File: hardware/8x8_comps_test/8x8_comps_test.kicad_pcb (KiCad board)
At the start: 2 copper layers, 408.6 x 315.4 mm, 250 parts

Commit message: Added test Schematic and PCB
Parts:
- removed ADC_3, ADC_4, ADC_5, ADC_6, ADC_7, ADC_8: MCP3008-I/P-DIP16, ADC:MCP3008-I&slash_P
- removed AMP_10, AMP_11, AMP_12, AMP_13, AMP_14, AMP_15, AMP_16, AMP_3, AMP_4, AMP_5, AMP_6, AMP_7, AMP_8, AMP_9: MCP619-I/SL, Op-Amp:footprints
- removed Addr_Sel_2, Addr_Sel_3, Addr_Sel_4, Addr_Sel_5, Addr_Sel_6: 100K, Resistor_THT:R_Axial_DIN0207_L6.3mm_D2.5mm_P7.62mm_Horizontal
- removed Amp_Fdbk_10, Amp_Fdbk_11, Amp_Fdbk_12, Amp_Fdbk_13, Amp_Fdbk_14, Amp_Fdbk_15, Amp_Fdbk_16, Amp_Fdbk_17, Amp_Fdbk_18, Amp_Fdbk_19, Amp_Fdbk_20, Amp_Fdbk_21, Amp_Fdbk_22, Amp_Fdbk_23, Amp_Fdbk_24, Amp_Fdbk_25, Amp_Fdbk_26, Amp_Fdbk_27, Amp_Fdbk_28, Amp_Fdbk_29, Amp_Fdbk_3, Amp_Fdbk_30, Amp_Fdbk_31, Amp_Fdbk_32, Amp_Fdbk_33, Amp_Fdbk_34, Amp_Fdbk_35, Amp_Fdbk_36, Amp_Fdbk_37, Amp_Fdbk_38, Amp_Fdbk_39, Amp_Fdbk_4, Amp_Fdbk_40, Amp_Fdbk_41, Amp_Fdbk_42, Amp_Fdbk_43, Amp_Fdbk_44, Amp_Fdbk_45, Amp_Fdbk_46, Amp_Fdbk_47, Amp_Fdbk_48, Amp_Fdbk_49, Amp_Fdbk_50, Amp_Fdbk_51, Amp_Fdbk_52, Amp_Fdbk_53, Amp_Fdbk_54, Amp_Fdbk_55, Amp_Fdbk_56, Amp_Fdbk_57, Amp_Fdbk_58, Amp_Fdbk_59, Amp_Fdbk_60, Amp_Fdbk_61, Amp_Fdbk_62, Amp_Fdbk_63, Amp_Fdbk_64, Amp_Fdbk_7, Amp_Fdbk_8, Amp_Fdbk_9: 2M, Resistor_THT:R_Axial_DIN0207_L6.3mm_D2.5mm_P7.62mm_Horizontal
- removed Drv_I_Sel_2, Drv_I_Sel_3, Drv_I_Sel_4, Drv_I_Sel_5, Drv_I_Sel_6, Drv_I_Sel_7, Drv_I_Sel_8: 2K, Resistor_THT:R_Axial_DIN0207_L6.3mm_D2.5mm_P7.62mm_Horizontal
- removed Drv_RST_PU_2, Drv_RST_PU_3, Drv_RST_PU_4, Drv_RST_PU_5, Drv_RST_PU_6, Drv_RST_PU_7, Drv_RST_PU_8: 10K, Resistor_THT:R_Axial_DIN0207_L6.3mm_D2.5mm_P7.62mm_Horizontal
- removed LD10, LD11, LD12, LD13, LD14, LD15, LD16, LD17, LD18, LD19, LD20, LD21, LD22, LD23, LD24, LD25, LD26, LD27, LD28, LD29, LD30, LD31, LD32, LD33, LD34, LD35, LD36, LD37, LD38, LD39, LD40, LD41, LD42, LD43, LD44, LD45, LD46, LD47, LD48, LD49, LD5, LD50, LD51, LD52, LD53, LD54, LD55, LD56, LD57, LD58, LD59, LD6, LD60, LD61, LD62, LD63, LD64, LD7, LD8, LD9: WP154A4SEJ3VBDZGC/CA, RGB LED:WP154A4SEJ3VBDZGC&slash_CA
- removed LED_Driver_2, LED_Driver_3, LED_Driver_4, LED_Driver_5, LED_Driver_6, LED_Driver_7, LED_Driver_8: PCA9956BTWY, LED Driver:SOP50P640X110-39N
- removed OC10, OC11, OC12, OC13, OC14, OC15, OC16, OC17, OC18, OC19, OC20, OC21, OC22, OC23, OC24, OC25, OC26, OC27, OC28, OC29, OC30, OC31, OC32, OC33, OC34, OC35, OC36, OC37, OC38, OC39, OC40, OC41, OC42, OC43, OC44, OC45, OC46, OC47, OC48, OC49, OC5, OC50, OC51, OC52, OC53, OC54, OC55, OC56, OC57, OC58, OC59, OC6, OC60, OC61, OC62, OC63, OC64, OC7, OC8, OC9: CPC1125N, Opto-coupler:footprints
- moved PH_1 337.6 mm to (41.9, 38.1), turned to 90 degrees
- moved DM 275.7 mm to (67.3, 74.9)
- moved Lvl_Sftr_1 264.4 mm to (81.3, 73.7), turned to 90 degrees
- moved Rev_Bias_Sel_1 262.4 mm to (78.7, 77.2), turned to 180 degrees
- moved Addr_Sel_1 236.4 mm to (62.2, 66.0), turned to 180 degrees
- moved Drv_I_Sel_1 221.2 mm to (64.8, 66.0), turned to 0 degrees
- moved LED_Driver_1 219.5 mm to (58.4, 74.9), turned to 0 degrees
- moved Drv_RST_PU_1 217.4 mm to (74.9, 66.0), turned to 0 degrees
- moved Amp_Fdbk_6 134.2 mm to (74.9, 52.1), turned to 0 degrees
- moved Amp_Fdbk_2 133.1 mm to (50.8, 52.1), turned to 0 degrees
- moved AMP_2 130.7 mm to (72.4, 44.5)
- moved OC1 129.5 mm to (40.6, 44.5)
- moved Amp_Fdbk_5 128.7 mm to (63.5, 52.1), turned to 0 degrees
- moved AMP_1 128.6 mm to (49.5, 44.5)
- moved ADC_2 128.1 mm to (72.4, 59.7), turned to -90 degrees
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- renumbered DEMUX_1 to DM, Pin_Header_1 to PH_1
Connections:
- net /LED Row IO 1/LDRow/LD1_B renamed /LED Row IO 1/LD1_TX_B
- net /LED Row IO 1/LDRow/LD1_G renamed /LED Row IO 1/LD1_TX_G
- net /LED Row IO 1/LDRow/LD2_B renamed /LED Row IO 1/LD2_TX_B
- net /LED Row IO 1/LDRow/LD2_G renamed /LED Row IO 1/LD2_TX_G
- net /LED Row IO 1/LDRow/LD3_B renamed /LED Row IO 2/LD1_TX_B
- net /LED Row IO 1/LDRow/LD3_G renamed /LED Row IO 2/LD1_TX_G
- net /LED Row IO 1/LDRow/LD4_B renamed /LED Row IO 2/LD2_TX_B
- net /LED Row IO 1/LDRow/LD4_G renamed /LED Row IO 2/LD2_TX_G
- net Net-(LED_Driver_1-Pad12) renamed /LED Row IO 2/LD1_TX_R
- net Net-(LED_Driver_1-Pad16) renamed /LED Row IO 2/LD2_TX_R
- net Net-(LED_Driver_1-Pad6) renamed /LED Row IO 1/LD1_TX_R
- net Net-(LED_Driver_1-Pad9) renamed /LED Row IO 1/LD2_TX_R
- ADC_1 pad 3: /LED Row IO 1/ LDRow_Amps/Amp_OP_3 -> unconnected-(ADC_1-Pad3)
- ADC_1 pad 4: /LED Row IO 1/ LDRow_Amps/Amp_OP_4 -> unconnected-(ADC_1-Pad4)
- ADC_1 pad 5: /LED Row IO 1/ LDRow_Amps/Amp_OP_5 -> unconnected-(ADC_1-Pad5)
- ADC_1 pad 6: /LED Row IO 1/ LDRow_Amps/Amp_OP_6 -> unconnected-(ADC_1-Pad6)
- ADC_1 pad 7: /LED Row IO 1/ LDRow_Amps/Amp_OP_7 -> unconnected-(ADC_1-Pad7)
- ADC_1 pad 8: /LED Row IO 1/ LDRow_Amps/Amp_OP_8 -> unconnected-(ADC_1-Pad8)
- ADC_2 pad 3: /LED Row IO 2/ LDRow_Amps/Amp_OP_3 -> unconnected-(ADC_2-Pad3)
- ADC_2 pad 4: /LED Row IO 2/ LDRow_Amps/Amp_OP_4 -> unconnected-(ADC_2-Pad4)
- ADC_2 pad 5: /LED Row IO 2/ LDRow_Amps/Amp_OP_5 -> unconnected-(ADC_2-Pad5)
- ADC_2 pad 6: /LED Row IO 2/ LDRow_Amps/Amp_OP_6 -> unconnected-(ADC_2-Pad6)
- ADC_2 pad 7: /LED Row IO 2/ LDRow_Amps/Amp_OP_7 -> unconnected-(ADC_2-Pad7)
- ADC_2 pad 8: /LED Row IO 2/ LDRow_Amps/Amp_OP_8 -> unconnected-(ADC_2-Pad8)
- AMP_1 pad 13: /LED Row IO 1/ LDRow_Amps/Amp_IP_4 -> unconnected-(AMP_1-Pad13)
- AMP_1 pad 14: /LED Row IO 1/ LDRow_Amps/Amp_OP_4 -> unconnected-(AMP_1-Pad14)
- AMP_1 pad 8: /LED Row IO 1/ LDRow_Amps/Amp_OP_3 -> unconnected-(AMP_1-Pad8)
- AMP_1 pad 9: /LED Row IO 1/ LDRow_Amps/Amp_IP_3 -> unconnected-(AMP_1-Pad9)
- AMP_2 pad 1: /LED Row IO 1/ LDRow_Amps/Amp_OP_5 -> /LED Row IO 2/ LDRow_Amps/Amp_OP_1
- AMP_2 pad 13: /LED Row IO 1/ LDRow_Amps/Amp_IP_8 -> unconnected-(AMP_2-Pad13)
- AMP_2 pad 14: /LED Row IO 1/ LDRow_Amps/Amp_OP_8 -> unconnected-(AMP_2-Pad14)
- AMP_2 pad 2: /LED Row IO 1/ LDRow_Amps/Amp_IP_5 -> /LED Row IO 2/ LDRow_Amps/Amp_IP_1
- AMP_2 pad 6: /LED Row IO 1/ LDRow_Amps/Amp_IP_6 -> /LED Row IO 2/ LDRow_Amps/Amp_IP_2
- AMP_2 pad 7: /LED Row IO 1/ LDRow_Amps/Amp_OP_6 -> /LED Row IO 2/ LDRow_Amps/Amp_OP_2
- AMP_2 pad 8: /LED Row IO 1/ LDRow_Amps/Amp_OP_7 -> unconnected-(AMP_2-Pad8)
- AMP_2 pad 9: /LED Row IO 1/ LDRow_Amps/Amp_IP_7 -> unconnected-(AMP_2-Pad9)
- Addr_Sel_1 pad 1: /LED Row IO 1/Drv_AD1 -> Net-(Addr_Sel_1-Pad1)
- Amp_Fdbk_5 pad 1: /LED Row IO 1/ LDRow_Amps/Amp_IP_5 -> /LED Row IO 2/ LDRow_Amps/Amp_IP_1
- Amp_Fdbk_5 pad 2: /LED Row IO 1/ LDRow_Amps/Amp_OP_5 -> /LED Row IO 2/ LDRow_Amps/Amp_OP_1
- Amp_Fdbk_6 pad 1: /LED Row IO 1/ LDRow_Amps/Amp_IP_6 -> /LED Row IO 2/ LDRow_Amps/Amp_IP_2
- Amp_Fdbk_6 pad 2: /LED Row IO 1/ LDRow_Amps/Amp_OP_6 -> /LED Row IO 2/ LDRow_Amps/Amp_OP_2
- DM pad 10: /LED Row IO 6/ADC_SHDN -> unconnected-(DEMUX_1-Pad10)
- DM pad 11: /LED Row IO 5/ADC_SHDN -> unconnected-(DEMUX_1-Pad11)
- DM pad 12: /LED Row IO 4/ADC_SHDN -> unconnected-(DEMUX_1-Pad12)
- DM pad 13: /LED Row IO 3/ADC_SHDN -> unconnected-(DEMUX_1-Pad13)
- DM pad 7: /LED Row IO 8/ADC_SHDN -> unconnected-(DEMUX_1-Pad7)
- DM pad 9: /LED Row IO 7/ADC_SHDN -> unconnected-(DEMUX_1-Pad9)
- LD3 pad 1: /LED Row IO 1/LDRow/LD3_R -> /LED Row IO 2/LDRow/LD1_R
- LD4 pad 1: /LED Row IO 1/LDRow/LD4_R -> /LED Row IO 2/LDRow/LD2_R
- LED_Driver_1 pad 2: /LED Row IO 1/Drv_AD0 -> Net-(Addr_Sel_1-Pad1)
- LED_Driver_1 pad 20: Net-(LED_Driver_1-Pad20) -> unconnected-(LED_Driver_1-Pad20)
- LED_Driver_1 pad 22: /LED Row IO 1/LDRow/LD5_G -> unconnected-(LED_Driver_1-Pad22)
- LED_Driver_1 pad 23: /LED Row IO 1/LDRow/LD5_B -> unconnected-(LED_Driver_1-Pad23)
- LED_Driver_1 pad 24: Net-(LED_Driver_1-Pad24) -> unconnected-(LED_Driver_1-Pad24)
- LED_Driver_1 pad 26: /LED Row IO 1/LDRow/LD6_G -> unconnected-(LED_Driver_1-Pad26)
- LED_Driver_1 pad 27: /LED Row IO 1/LDRow/LD6_B -> unconnected-(LED_Driver_1-Pad27)
- LED_Driver_1 pad 28: Net-(LED_Driver_1-Pad28) -> unconnected-(LED_Driver_1-Pad28)
- LED_Driver_1 pad 29: /LED Row IO 1/LDRow/LD7_G -> unconnected-(LED_Driver_1-Pad29)
- LED_Driver_1 pad 3: /LED Row IO 1/Drv_AD1 -> unconnected-(LED_Driver_1-Pad3)
- LED_Driver_1 pad 30: /LED Row IO 1/LDRow/LD7_B -> unconnected-(LED_Driver_1-Pad30)
- LED_Driver_1 pad 31: Net-(LED_Driver_1-Pad31) -> unconnected-(LED_Driver_1-Pad31)
- LED_Driver_1 pad 32: /LED Row IO 1/LDRow/LD8_G -> unconnected-(LED_Driver_1-Pad32)
- LED_Driver_1 pad 33: /LED Row IO 1/LDRow/LD8_B -> unconnected-(LED_Driver_1-Pad33)
- OC3 pad 1: /LED Row IO 1/LDRow/LD3_R -> /LED Row IO 2/LDRow/LD1_R
- OC3 pad 3: /LED Row IO 1/ LDRow_Amps/Amp_IP_3 -> /LED Row IO 2/ LDRow_Amps/Amp_IP_1
- OC3 pad 4: /LED Row IO 1/LDRow/LD3_R -> /LED Row IO 2/LDRow/LD1_R
- OC4 pad 1: /LED Row IO 1/LDRow/LD4_R -> /LED Row IO 2/LDRow/LD2_R
- OC4 pad 3: /LED Row IO 1/ LDRow_Amps/Amp_IP_4 -> /LED Row IO 2/ LDRow_Amps/Amp_IP_2
- OC4 pad 4: /LED Row IO 1/LDRow/LD4_R -> /LED Row IO 2/LDRow/LD2_R
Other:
- board size 408.6 x 315.4 mm -> 47.8 x 47.5 mm

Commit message: Changed Test Layout
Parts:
- moved Rev_Bias_Sel_1 48.3 mm to (50.8, 37.8)
- moved Drv_RST_PU_1 37.5 mm to (40.6, 50.8), turned to 90 degrees
- moved PH_1 37.0 mm to (78.7, 34.3), turned to 0 degrees
- moved Drv_I_Sel_1 36.0 mm to (40.6, 39.4), turned to 90 degrees
- moved DM 33.8 mm to (48.3, 47.0)
- moved OC4 26.2 mm to (55.9, 50.8), turned to -90 degrees
- moved ADC_2 25.3 mm to (64.8, 35.6), turned to 90 degrees
- moved Addr_Sel_1 21.9 mm to (40.6, 62.2), turned to 90 degrees
- moved ADC_1 21.6 mm to (64.8, 74.9)
- moved Amp_Fdbk_1 21.6 mm to (54.6, 67.3)
- moved Amp_Fdbk_2 21.6 mm to (66.0, 67.3)
- moved OC1 21.6 mm to (55.9, 59.7)
- moved AMP_1 21.6 mm to (64.8, 59.7)
- moved OC2 21.6 mm to (73.7, 59.7)
- moved LED_Driver_1 19.4 mm to (48.3, 58.4)
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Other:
- board size 47.8 x 47.5 mm -> 47.8 x 51.3 mm

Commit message: Updated Components
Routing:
- net +5V: track 0.00 -> 190.6 mm, vias 0 -> 2
- net GND: track 0.00 -> 158.2 mm
- net SPI_MISO_5V: track 0.00 -> 84.0 mm
- net SPI_SCK: track 0.00 -> 67.8 mm
- net RB Voltage: track 0.00 -> 64.5 mm, vias 0 -> 1
- net SPI_MOSI: track 0.00 -> 64.1 mm, vias 0 -> 1
- net /LED Row IO 2/LDRow/LD1_R: track 0.00 -> 59.4 mm
- net +9V: track 0.00 -> 56.8 mm, vias 0 -> 1
- net I2C_SDA_5V: track 0.00 -> 49.7 mm, vias 0 -> 1
- net SPI_SS_0: track 0.00 -> 46.3 mm, vias 0 -> 1
- net SPI_SS_1: track 0.00 -> 43.0 mm, vias 0 -> 1
- net /LED Row IO 1/ADC_SHDN: track 0.00 -> 40.1 mm
- net I2C_SCL: track 0.00 -> 38.8 mm, vias 0 -> 1
- net +3V3: track 0.00 -> 38.1 mm
- net SPI_SS_2: track 0.00 -> 37.5 mm, vias 0 -> 1
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
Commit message: Updated Footprints
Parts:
- removed ADC_1, ADC_2: MCP3008-I/P-DIP16, ADC:MCP3008-I&slash_P
- removed AMP_1, AMP_2: MCP619-I/SL, Op-Amp:footprints
- removed Addr_Sel_1: 100K, Resistor_THT:R_Axial_DIN0207_L6.3mm_D2.5mm_P7.62mm_Horizontal
- removed Amp_Fdbk_1, Amp_Fdbk_2, Amp_Fdbk_5, Amp_Fdbk_6: 2M, Resistor_THT:R_Axial_DIN0207_L6.3mm_D2.5mm_P7.62mm_Horizontal
- removed DM: 74HC138D-Q100,118, DEMUX:footprints
- removed Drv_I_Sel_1: 2K, Resistor_THT:R_Axial_DIN0207_L6.3mm_D2.5mm_P7.62mm_Horizontal
- removed Drv_RST_PU_1: 10K, Resistor_THT:R_Axial_DIN0207_L6.3mm_D2.5mm_P7.62mm_Horizontal
- removed LD1, LD2, LD3, LD4: WP154A4SEJ3VBDZGC/CA, RGB LED:WP154A4SEJ3VBDZGC&slash_CA
- removed LED_Driver_1: PCA9956BTWY, LED Driver:SOP50P640X110-39N
- removed Lvl_Sftr_1: LSF0102DCH, Level Shifter:LSF0102DCH
- removed OC1, OC2, OC3, OC4: CPC1125N, Opto-coupler:footprints
- removed PH_1: Conn_02x16_Odd_Even, Connector_PinHeader_2.54mm:PinHeader_2x16_P2.54mm_Vertical
- removed Rev_Bias_Sel_1: 100K, Potentiometer_THT:Potentiometer_Runtron_RM-065_Vertical
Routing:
- net +5V: track 190.6 -> 0.00 mm, vias 2 -> 0
- net GND: track 158.2 -> 0.00 mm
- net SPI_MISO_5V: track 84.0 -> 0.00 mm
- net SPI_SCK: track 67.8 -> 0.00 mm
- net RB Voltage: track 64.5 -> 0.00 mm, vias 1 -> 0
- net SPI_MOSI: track 64.1 -> 0.00 mm, vias 1 -> 0
- net /LED Row IO 2/LDRow/LD1_R: track 59.4 -> 0.00 mm
- net +9V: track 56.8 -> 0.00 mm, vias 1 -> 0
- net I2C_SDA_5V: track 49.7 -> 0.00 mm, vias 1 -> 0
- net SPI_SS_0: track 46.3 -> 0.00 mm, vias 1 -> 0
- net SPI_SS_1: track 43.0 -> 0.00 mm, vias 1 -> 0
- net /LED Row IO 1/ADC_SHDN: track 40.1 -> 0.00 mm
- net I2C_SCL: track 38.8 -> 0.00 mm, vias 1 -> 0
- net +3V3: track 38.1 -> 0.00 mm
- net SPI_SS_2: track 37.5 -> 0.00 mm, vias 1 -> 0
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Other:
- board outline removed

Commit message: Updated Placement
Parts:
- added ADC_1: MCP3008-I/P-DIP16, ADC:MCP3008-I&slash_P, B.Cu at (29.2, 70.6)
- added ADC_2: MCP3008-I/P-DIP16, ADC:MCP3008-I&slash_P, F.Cu at (47.0, 70.6)
- added AMP_1: MCP619-I/SL, Op-Amp:footprints, F.Cu at (38.1, 64.8)
- added AMP_2: MCP619-I/SL, Op-Amp:footprints, B.Cu at (38.1, 64.8)
- added Addr_Sel_1: 100K, Resistor_THT:R_Axial_DIN0207_L6.3mm_D2.5mm_P7.62mm_Horizontal, F.Cu at (45.7, 83.8)
- added Amp_Fdbk_1: 2M, Resistor_THT:R_Axial_DIN0207_L6.3mm_D2.5mm_P7.62mm_Horizontal, F.Cu at (25.4, 83.8)
- added Amp_Fdbk_2: 2M, Resistor_THT:R_Axial_DIN0207_L6.3mm_D2.5mm_P7.62mm_Horizontal, F.Cu at (35.6, 83.8)
- added Amp_Fdbk_3: 2M, Resistor_THT:R_Axial_DIN0207_L6.3mm_D2.5mm_P7.62mm_Horizontal, B.Cu at (53.3, 68.6)
- added Amp_Fdbk_4: 2M, Resistor_THT:R_Axial_DIN0207_L6.3mm_D2.5mm_P7.62mm_Horizontal, B.Cu at (53.3, 80.0)
- added DEMUX_1: 74HC138D-Q100,118, DEMUX:footprints, F.Cu at (38.1, 76.2)
- added Drv_I_Sel_1: 2K, Resistor_THT:R_Axial_DIN0207_L6.3mm_D2.5mm_P7.62mm_Horizontal, B.Cu at (48.3, 88.9)
- added Drv_RST_PU_1: 10K, Resistor_THT:R_Axial_DIN0207_L6.3mm_D2.5mm_P7.62mm_Horizontal, B.Cu at (52.1, 87.6)
- added LD1: WP154A4SEJ3VBDZGC/CA, RGB LED:WP154A4SEJ3VBDZGC&slash_CA, F.Cu at (27.9, 90.2)
- added LD2: WP154A4SEJ3VBDZGC/CA, RGB LED:WP154A4SEJ3VBDZGC&slash_CA, F.Cu at (35.6, 90.2)
- added LD3: WP154A4SEJ3VBDZGC/CA, RGB LED:WP154A4SEJ3VBDZGC&slash_CA, F.Cu at (27.9, 97.8)
- added LD4: WP154A4SEJ3VBDZGC/CA, RGB LED:WP154A4SEJ3VBDZGC&slash_CA, F.Cu at (35.6, 97.8)
- added LED_Driver_1: PCA9956BTWY, LED Driver:SOP50P640X110-39N, B.Cu at (38.1, 76.2)
- added Lvl_Sftr_1: LSF0102DCH, Level Shifter:LSF0102DCH, F.Cu at (52.1, 97.8)
- added Pin_Header_1: Conn_02x16_Odd_Even, Connector_PinHeader_2.54mm:PinHeader_2x16_P2.54mm_Vertical, B.Cu at (59.7, 61.0)
- added Rev_Bias_Sel_1: 100K, Potentiometer_THT:Potentiometer_Runtron_RM-065_Vertical, B.Cu at (47.0, 94.3)
- added SSR1: TLP417A-TP-F, SSR:footprints, F.Cu at (29.2, 64.3)
- added SSR2: TLP417A-TP-F, SSR:footprints, F.Cu at (29.2, 77.0)
- added SSR3: TLP417A-TP-F, SSR:footprints, B.Cu at (47.0, 64.3)
- added SSR4: TLP417A-TP-F, SSR:footprints, B.Cu at (47.0, 75.7)
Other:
- board outline added: 38.1 x 43.2 mm

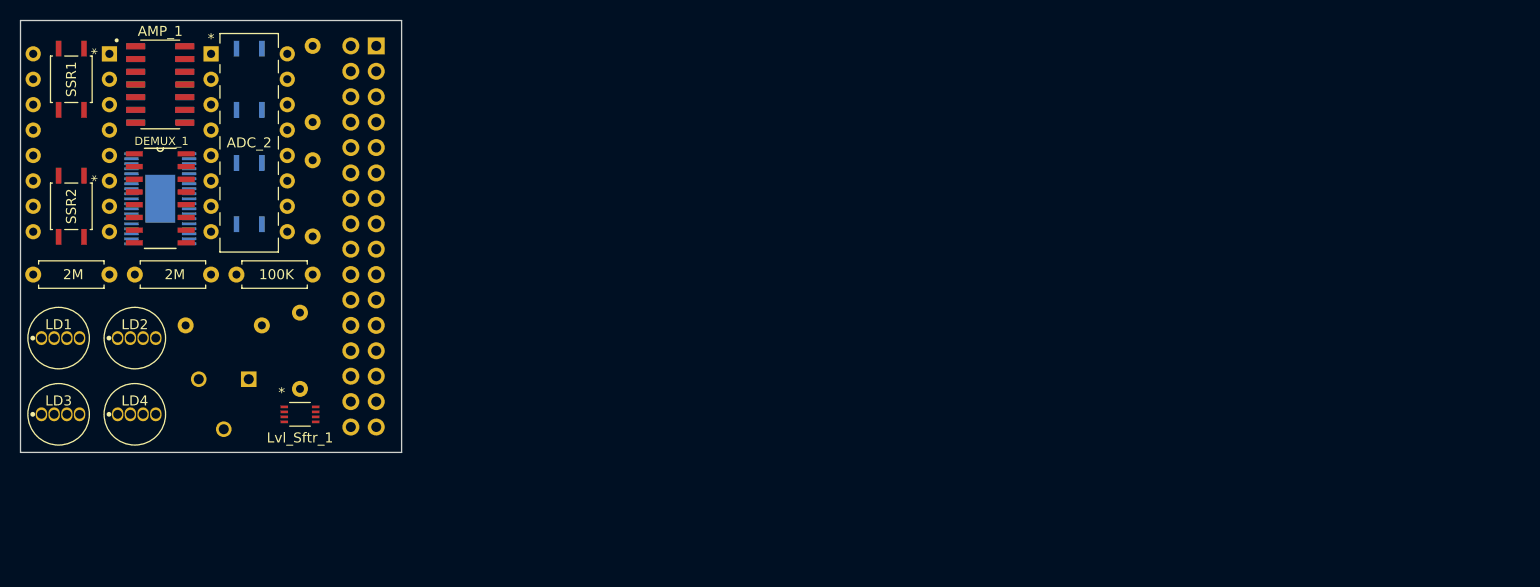
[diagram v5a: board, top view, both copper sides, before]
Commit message: Designed PCB for Components Test
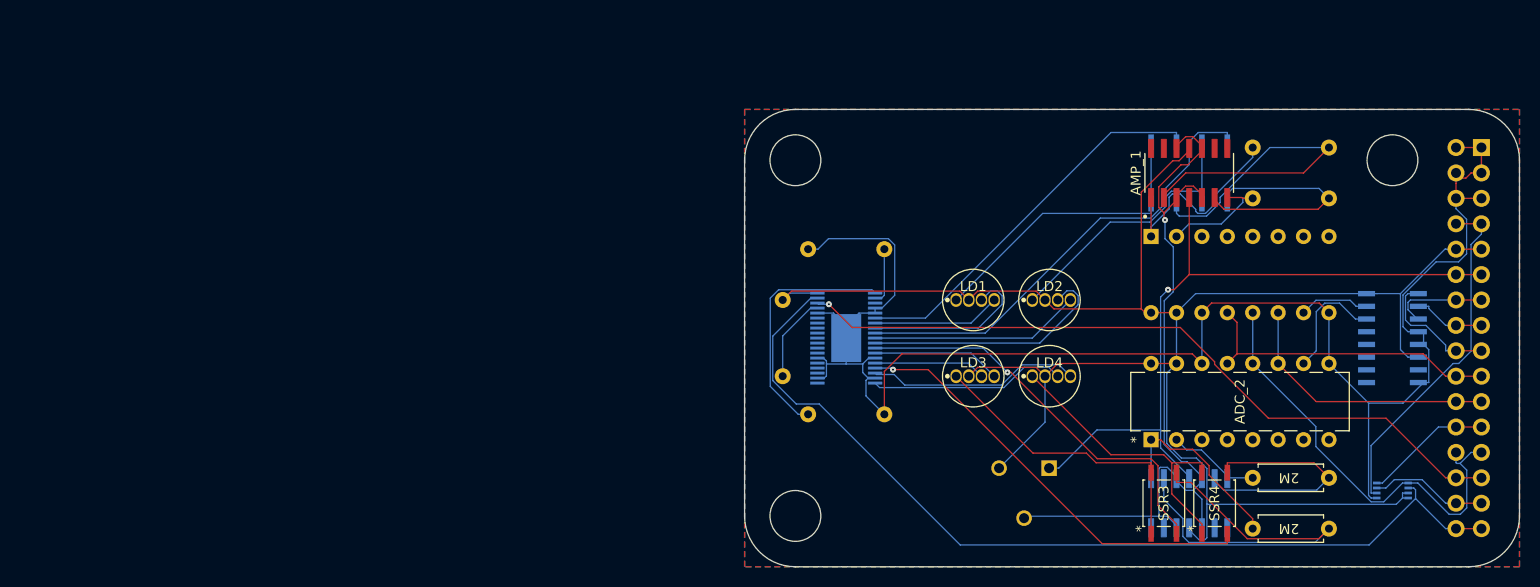
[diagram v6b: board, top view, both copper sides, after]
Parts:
- Addr_Sel_1, Amp_Fdbk_1, Amp_Fdbk_2, DEMUX_1, Lvl_Sftr_1, SSR1, SSR2: moved to B.Cu
- Amp_Fdbk_3, Amp_Fdbk_4, SSR3, SSR4: moved to F.Cu
- moved Amp_Fdbk_1 130.2 mm to (154.9, 71.1), turned to 180 degrees
- moved DEMUX_1 124.0 mm to (161.3, 90.2), turned to 180 degrees
- moved Amp_Fdbk_2 119.6 mm to (154.9, 76.2), turned to 180 degrees
- moved ADC_1 117.6 mm to (146.1, 83.8), turned to -90 degrees
- moved SSR2 114.3 mm to (143.5, 73.7)
- moved AMP_2 111.1 mm to (141.0, 106.7), turned to -90 degrees
- moved Pin_Header_1 111.0 mm to (170.2, 71.1)
- moved SSR1 109.6 mm to (138.4, 73.7)
- moved Lvl_Sftr_1 109.5 mm to (161.3, 105.4)
- moved Amp_Fdbk_3 109.4 mm to (154.9, 109.2), turned to 180 degrees
- moved Amp_Fdbk_4 104.4 mm to (154.9, 104.1), turned to 180 degrees
- moved AMP_1 103.2 mm to (141.0, 73.7), turned to 90 degrees
- moved ADC_2 102.4 mm to (146.1, 96.5), turned to 90 degrees
- moved SSR4 101.4 mm to (143.5, 106.7), turned to 90 degrees
- moved SSR3 100.8 mm to (138.4, 106.7), turned to 90 degrees
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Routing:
- net +5V: track 0.00 -> 186.8 mm
- net GND: track 0.00 -> 165.6 mm
- net I2C_SDA_5V: track 0.00 -> 93.0 mm
- net RB Voltage: track 0.00 -> 78.8 mm, vias 0 -> 1
- net I2C_SCL: track 0.00 -> 73.8 mm, vias 0 -> 1
- net +9V: track 0.00 -> 72.8 mm, vias 0 -> 1
- net /LED Row IO 1/LD2_TX_R: track 0.00 -> 46.7 mm
- net SPI_MISO_5V: track 0.00 -> 44.5 mm
- net /LED Row IO 2/LD2_TX_R: track 0.00 -> 43.5 mm, vias 0 -> 1
- net /LED Row IO 2/ LDRow_Amps/Amp_IP_1: track 0.00 -> 41.0 mm
- net /LED Row IO 2/LD1_TX_R: track 0.00 -> 40.7 mm, vias 0 -> 1
- net /LED Row IO 1/LD1_TX_R: track 0.00 -> 38.8 mm
- net /LED Row IO 1/ LDRow_Amps/Amp_IP_1: track 0.00 -> 38.2 mm
- net +3V3: track 0.00 -> 34.9 mm
- net SPI_SCK: track 0.00 -> 31.2 mm
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- added copper zone on B.Cu, net GND
- added copper zone on F.Cu, net GND
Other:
- board size 38.1 x 43.2 mm -> 77.5 x 45.7 mm

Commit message: Updated PCB
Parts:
- removed ADC_1, ADC_2: MCP3008-I/P-DIP16, ADC:MCP3008-I&slash_P
- removed AMP_1, AMP_2: MCP619-I/SL, Op-Amp:footprints
- removed Addr_Sel_1: 100K, Resistor_THT:R_Axial_DIN0207_L6.3mm_D2.5mm_P7.62mm_Horizontal
- removed Amp_Fdbk_1, Amp_Fdbk_2, Amp_Fdbk_3, Amp_Fdbk_4: 2M, Resistor_THT:R_Axial_DIN0207_L6.3mm_D2.5mm_P7.62mm_Horizontal
- removed DEMUX_1: 74HC138D-Q100,118, DEMUX:footprints
- removed Drv_I_Sel_1: 2K, Resistor_THT:R_Axial_DIN0207_L6.3mm_D2.5mm_P7.62mm_Horizontal
- removed Drv_RST_PU_1: 10K, Resistor_THT:R_Axial_DIN0207_L6.3mm_D2.5mm_P7.62mm_Horizontal
- removed LED_Driver_1: PCA9956BTWY, LED Driver:SOP50P640X110-39N
- removed Lvl_Sftr_1: LSF0102DCH, Level Shifter:LSF0102DCH
- removed Pin_Header_1: Conn_02x16_Odd_Even, Connector_PinHeader_2.54mm:PinHeader_2x16_P2.54mm_Vertical
- removed Rev_Bias_Sel_1: 100K, Potentiometer_THT:Potentiometer_Runtron_RM-065_Vertical
- added ADC1: MCP3008-I/P-DIP16, ADC:MCP3008-I&slash_P, F.Cu at (72.4, 84.2)
- added AMP1: MCP619-I/SL, Op-Amp:footprints, F.Cu at (91.9, 88.4)
- added AMP2: MCP619-I/SL, Op-Amp:footprints, F.Cu at (82.1, 88.4)
- added DRV1: PCA9956BTWY, LED Driver:SOP50P640X110-39N, B.Cu at (101.8, 88.4)
- added FDB1: 2M, Resistor - Through-Hole:footprints, F.Cu at (91.9, 93.6)
- added FDB2: 2M, Resistor - Through-Hole:footprints, F.Cu at (91.9, 83.2)
- added FDB3: 2M, Resistor - Through-Hole:footprints, F.Cu at (82.1, 93.6)
- added FDB4: 2M, Resistor - Through-Hole:footprints, F.Cu at (82.1, 83.2)
- added ISEL1: 2K, Resistor - Through-Hole:footprints, F.Cu at (101.7, 83.0)
- added PH1: Conn_02x11_Odd_Even, Connector_PinSocket_2.54mm:PinSocket_2x11_P2.54mm_Vertical, B.Cu at (87.8, 79.3)
- added PU1: 10K, Resistor - Through-Hole:footprints, F.Cu at (101.7, 93.8)
- added RBSEL1: 100K, Potentiometer_THT:Potentiometer_Runtron_RM-065_Vertical, B.Cu at (84.3, 75.2)
- added SFTR1: VSSOP8_SOT765-1_NEX, Level Shifter:LSF0102DCH, B.Cu at (72.5, 83.3)
- SSR3, SSR4: moved to B.Cu
- moved SSR4 63.4 mm to (82.1, 90.7), turned to 180 degrees
- moved SSR3 60.0 mm to (82.1, 86.0), turned to 0 degrees
- moved SSR2 54.3 mm to (91.9, 90.7), turned to 180 degrees
- moved SSR1 48.1 mm to (91.9, 86.0), turned to 0 degrees
- moved LD2 18.0 mm to (110.0, 92.2)
- moved LD3 9.56 mm to (117.6, 84.6)
- moved LD1 9.56 mm to (110.0, 84.6)
- moved LD4 9.56 mm to (117.6, 92.2)
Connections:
- net /LED Row IO 1/LDRow/LD1_R renamed /LDRow/LD1_R
- net /LED Row IO 1/LDRow/LD2_R renamed /LDRow/LD2_R
- net /LED Row IO 2/LDRow/LD1_R renamed /LDRow1/LD1_R
- net /LED Row IO 2/LDRow/LD2_R renamed /LDRow1/LD2_R
- LD1 pad 3: /LED Row IO 1/LD1_TX_B -> /LDRow/LD1_B
- LD1 pad 4: /LED Row IO 1/LD1_TX_G -> /LDRow/LD1_G
- LD2 pad 3: /LED Row IO 1/LD2_TX_B -> /LDRow/LD2_B
- LD2 pad 4: /LED Row IO 1/LD2_TX_G -> /LDRow/LD2_G
- LD3 pad 3: /LED Row IO 2/LD1_TX_B -> /LDRow1/LD1_B
- LD3 pad 4: /LED Row IO 2/LD1_TX_G -> /LDRow1/LD1_G
- LD4 pad 3: /LED Row IO 2/LD2_TX_B -> /LDRow1/LD2_B
- LD4 pad 4: /LED Row IO 2/LD2_TX_G -> /LDRow1/LD2_G
- SSR1 pad 2: /LED Row IO 1/LD1_TX_R -> Net-(DRV1-Pad6)
- SSR1 pad 3: /LED Row IO 1/ LDRow_Amps/Amp_IP_1 -> Net-(AMP1-Pad9)
- SSR2 pad 2: /LED Row IO 1/LD2_TX_R -> Net-(DRV1-Pad33)
- SSR2 pad 3: /LED Row IO 1/ LDRow_Amps/Amp_IP_2 -> Net-(AMP1-Pad6)
- SSR3 pad 2: /LED Row IO 2/LD1_TX_R -> Net-(DRV1-Pad7)
- SSR3 pad 3: /LED Row IO 2/ LDRow_Amps/Amp_IP_1 -> Net-(AMP2-Pad13)
- SSR4 pad 2: /LED Row IO 2/LD2_TX_R -> Net-(DRV1-Pad32)
- SSR4 pad 3: /LED Row IO 2/ LDRow_Amps/Amp_IP_2 -> Net-(AMP2-Pad2)
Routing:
- net I2C_SDA_5V: track 93.0 -> 29.0 mm
- net +5V: track 186.8 -> 139.6 mm
- net /LED Row IO 1/LD2_TX_R: track 46.7 -> 0.00 mm
- net /LED Row IO 2/LD2_TX_R: track 43.5 -> 0.00 mm, vias 1 -> 0
- net /LED Row IO 2/ LDRow_Amps/Amp_IP_1: track 41.0 -> 0.00 mm
- net /LED Row IO 2/LD1_TX_R: track 40.7 -> 0.00 mm, vias 1 -> 0
- net /LED Row IO 1/LD1_TX_R: track 38.8 -> 0.00 mm
- net SPI_MISO_5V: track 44.5 -> 5.80 mm
- net /LED Row IO 1/ LDRow_Amps/Amp_IP_1: track 38.2 -> 0.00 mm
- net RB Voltage: track 78.8 -> 41.8 mm, vias 1 -> 0
- net GND: track 165.6 -> 130.9 mm
- net I2C_SDA_3V3: track 11.8 -> 42.4 mm
- net +9V: track 72.8 -> 45.1 mm, vias 1 -> 0
- net SPI_MISO_3V3: track 12.8 -> 39.3 mm
- net /LED Row IO 1/LD2_TX_B: track 25.4 -> 0.00 mm
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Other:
- board size 77.5 x 45.7 mm -> 54.5 x 23.2 mm
